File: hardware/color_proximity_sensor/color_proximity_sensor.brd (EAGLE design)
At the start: 48 x 24.8 mm, 69 parts, among them IC1 TCS37725FN, IC2 APDS-9800-021, IC4 LM25011MY, IC5 ATXMEGA64DA-AU, J1 PDI_ATMEL_WIDTH, Q1 16 MHz, T1 BC847CDXV6T1G, T4 BC847CDXV6T1G

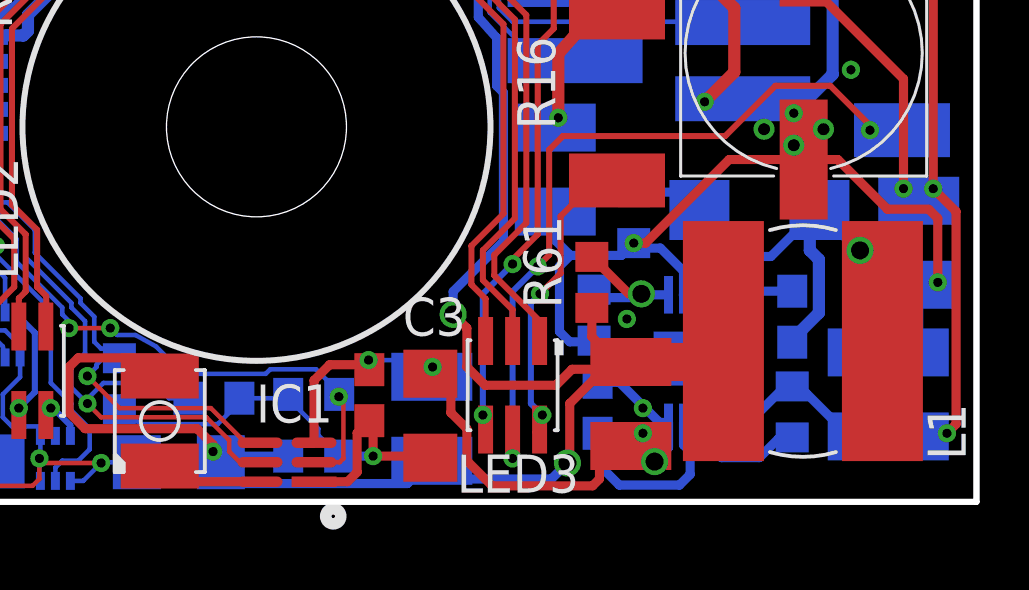
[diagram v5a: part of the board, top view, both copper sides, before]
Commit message: corrected tcs37725 and b160, need rerouting tcs37725
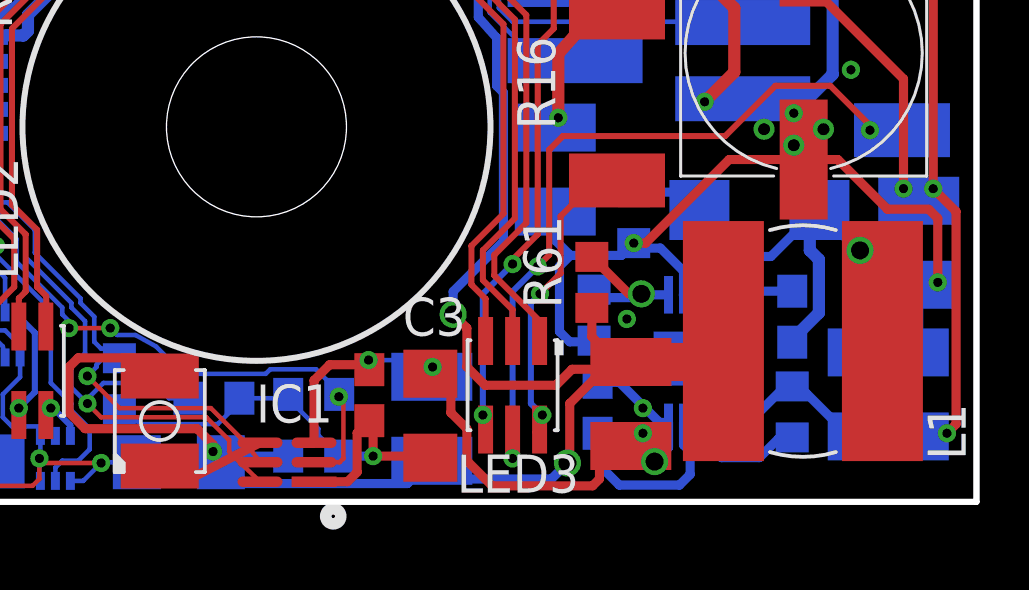
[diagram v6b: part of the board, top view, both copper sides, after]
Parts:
- turned D8 to 0 degrees
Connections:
- net INT_TCS37725_3V3: now also IC1.5; no longer IC1.4
- net N$38: now also D8.C; no longer D8.A
- net N$39: now also D8.A; no longer D8.C
- net N$4: now also IC1.4; no longer IC1.6
- net SDA_3V3: now also IC1.6; no longer IC1.5
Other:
- board text added: "color_prox sens v2"
- board text removed: "color_prox sens v1"
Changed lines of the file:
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@@
 <layers>
 <layer number="1" name="Top" color="4" fill="1" visible="yes" active="yes"/>
-<layer number="16" name="Bottom" color="1" fill="1" visible="yes" active="yes"/>
+<layer number="16" name="Bottom" color="1" fill="1" visible="no" active="yes"/>
 <layer number="17" name="Pads" color="2" fill="1" visible="yes" active="yes"/>
 <layer number="18" name="Vias" color="2" fill="1" visible="yes" active="yes"/>
@@
 <layer number="23" name="tOrigins" color="15" fill="1" visible="yes" active="yes"/>
 <layer number="24" name="bOrigins" color="15" fill="1" visible="yes" active="yes"/>
-<layer number="25" name="tNames" color="7" fill="1" visible="yes" active="yes"/>
+<layer number="25" name="tNames" color="7" fill="1" visible="no" active="yes"/>
 <layer number="26" name="bNames" color="7" fill="1" visible="yes" active="yes"/>
 <layer number="27" name="tValues" color="7" fill="1" visible="no" active="yes"/>
@@
 <layer number="42" name="bRestrict" color="1" fill="10" visible="yes" active="yes"/>
 <layer number="43" name="vRestrict" color="2" fill="10" visible="yes" active="yes"/>
-<layer number="44" name="Drills" color="7" fill="1" visible="yes" active="yes"/>
-<layer number="45" name="Holes" color="7" fill="1" visible="yes" active="yes"/>
+<layer number="44" name="Drills" color="7" fill="1" visible="no" active="yes"/>
+<layer number="45" name="Holes" color="7" fill="1" visible="no" active="yes"/>
 <layer number="46" name="Milling" color="3" fill="1" visible="no" active="yes"/>
 <layer number="47" name="Measures" color="7" fill="1" visible="no" active="yes"/>
@@
 <circle x="24" y="12.5" radius="7.8" width="0.2032" layer="42"/>
 <text x="31.8516" y="20.193" size="1.778" layer="26" rot="MR0">color_prox
-sens v1</text>
+sens v2</text>
 <circle x="24" y="12.5" radius="9" width="0.4064" layer="47"/>
 <circle x="24" y="12.5" radius="7.8" width="0.2" layer="22"/>
@@
 <attribute name="MOUSER" value="581-1210ZG226Z" x="36.479478125" y="3.261359375" size="1.778" layer="27" rot="R270" display="off"/>
 </element>
-<element name="D8" library="robotter_diode" package="SMA" value="B160-13F" x="40.767" y="9.7282" smashed="yes" rot="MR180">
-<attribute name="RS" value="738-4765" x="110.617" y="35.1282" size="1.778" layer="28" rot="MR180" display="off"/>
-<attribute name="NAME" x="40.1762" y="8.7562" size="1.27" layer="26" ratio="10" rot="MR90"/>
-<attribute name="VALUE" x="38.017" y="13.2282" size="1.27" layer="28" ratio="10" rot="MR180"/>
-<attribute name="MOUSER" value="621-B160-F" x="40.767" y="9.7282" size="1.778" layer="28" rot="MR180" display="off"/>
+<element name="D8" library="robotter_diode" package="SMA" value="B160-13F" x="40.767" y="9.7282" smashed="yes" rot="MR0">
+<attribute name="RS" value="738-4765" x="-29.083" y="-15.6718" size="1.778" layer="28" rot="MR0" display="off"/>
+<attribute name="NAME" x="41.3578" y="10.7002" size="1.27" layer="26" ratio="10" rot="MR270"/>
+<attribute name="VALUE" x="43.517" y="6.2282" size="1.27" layer="28" ratio="10" rot="MR0"/>
+<attribute name="MOUSER" value="621-B160-F" x="40.767" y="9.7282" size="1.778" layer="28" rot="MR0" display="off"/>
 </element>
 <element name="L1" library="robotter_inductor" package="SDR0805" value="SDR0805-270KL" x="42.2148" y="5.3594" smashed="yes" rot="R90">
@@
 <attribute name="NAME" x="2.6416" y="21.4122" size="1.27" layer="26" rot="MR90"/>
 <attribute name="VALUE" x="-1.0922" y="22.098" size="1.27" layer="28" rot="MR90"/>
-<attribute name="MOUSER" value="652-CR0805FX-1502ELF" x="1.4478" y="22.733" size="1.778" layer="28" rot="MR90" display="off"/>
+<attribute name="MOUSER" value="660-RK73H2ATTD1502F" x="1.4478" y="22.733" size="1.778" layer="28" rot="MR90" display="off"/>
 </element>
 <element name="R14" library="robotter_resistor" package="R0805" value="1k" x="1.4478" y="22.7076" smashed="yes" rot="R270">
@@
 <attribute name="NAME" x="26.543" y="2.159" size="1.27" layer="100" rot="MR0"/>
 <attribute name="VALUE" x="26.543" y="-0.381" size="1.27" layer="28" rot="MR0"/>
-<attribute name="MOUSER" value="279-CRG0603F22R" x="25.908" y="1.524" size="1.778" layer="28" rot="MR0" display="off"/>
+<attribute name="MOUSER" value="660-RK73H1JTTD22R0F" x="25.908" y="1.524" size="1.778" layer="28" rot="MR0" display="off"/>
 </element>
 <element name="IC2" library="robotter_ic" package="APDS-9800" value="APDS-9800-021" x="10.3886" y="4.9022" smashed="yes">
@@
 <attribute name="NAME" x="10.9474" y="2.794" size="1.27" layer="103" rot="MR0"/>
 <attribute name="VALUE" x="10.6426" y="1.4732" size="1.27" layer="28" rot="MR0"/>
-<attribute name="MOUSER" value="279-CRG0603F22R" x="10.0076" y="3.3782" size="1.778" layer="28" rot="MR0" display="off"/>
+<attribute name="MOUSER" value="660-RK73H1JTTD22R0F" x="10.0076" y="3.3782" size="1.778" layer="28" rot="MR0" display="off"/>
 </element>
 <element name="R4" library="robotter_resistor" package="R0603" value="22 ohms" x="10.0076" y="1.3462" smashed="yes" rot="MR0">
@@
 <attribute name="NAME" x="11.176" y="0.762" size="1.27" layer="103" rot="MR0"/>
 <attribute name="VALUE" x="10.6426" y="-0.5588" size="1.27" layer="28" rot="MR0"/>
-<attribute name="MOUSER" value="279-CRG0603F22R" x="10.0076" y="1.3462" size="1.778" layer="28" rot="MR0" display="off"/>
+<attribute name="MOUSER" value="660-RK73H1JTTD22R0F" x="10.0076" y="1.3462" size="1.778" layer="28" rot="MR0" display="off"/>
 </element>
 <element name="R5" library="robotter_resistor" package="R0603" value="10K-F" x="11.9126" y="9.7282" smashed="yes">
@@
 <signal name="N$38">
 <contactref element="IC4" pad="9"/>
-<contactref element="D8" pad="A"/>
+<contactref element="D8" pad="C"/>
 <contactref element="C32" pad="2"/>
 <contactref element="L1" pad="1"/>
@@
 <signal name="N$39">
 <contactref element="IC4" pad="8"/>
-<contactref element="D8" pad="C"/>
+<contactref element="D8" pad="A"/>
 <contactref element="R22" pad="2"/>
 <wire x1="38.735" y1="6.9022" x2="38.735" y2="9.6962" width="0.3048" layer="16"/>
@@
 <signal name="INT_TCS37725_3V3">
 <contactref element="R1" pad="1"/>
-<contactref element="IC1" pad="4"/>
+<contactref element="IC1" pad="5"/>
 <contactref element="IC5" pad="27"/>
 <wire x1="19.431" y1="4.787" x2="19.265" y2="4.953" width="0.1524" layer="16"/>
@@
 <wire x1="19.3684" y1="4.787" x2="19.431" y2="4.787" width="0.1524" layer="16"/>
 <wire x1="22.479" y1="3.1242" x2="23.6324" y2="1.9708" width="0.1524" layer="1"/>
-<wire x1="23.6324" y1="1.9708" x2="24.119" y2="1.9708" width="0.1524" layer="1"/>
+<wire x1="23.6324" y1="1.9708" x2="24.119" y2="1.3208" width="0.1524" layer="1"/>
 </signal>
 <signal name="SDA_3V3">
-<contactref element="IC1" pad="5"/>
+<contactref element="IC1" pad="6"/>
 <contactref element="R25" pad="1"/>
 <contactref element="IC5" pad="28"/>
@@
 <wire x1="23.0886" y1="2.0574" x2="23.0886" y2="1.6764" width="0.1524" layer="1"/>
 <wire x1="23.0886" y1="1.6764" x2="23.4442" y2="1.3208" width="0.1524" layer="1"/>
-<wire x1="23.4442" y1="1.3208" x2="24.119" y2="1.3208" width="0.1524" layer="1"/>
+<wire x1="23.4442" y1="1.3208" x2="24.119" y2="0.6708" width="0.1524" layer="1"/>
 </signal>
 <signal name="SCL_3V3">
@@
 </signal>
 <signal name="N$4">
-<contactref element="IC1" pad="6"/>
+<contactref element="IC1" pad="4"/>
 <contactref element="LED1" pad="C"/>
 <wire x1="21.2076" y1="1.0668" x2="20.7772" y2="1.1924" width="0.3048" layer="1"/>
 <wire x1="21.2076" y1="1.0668" x2="21.6036" y2="0.6708" width="0.3048" layer="1"/>
-<wire x1="21.6036" y1="0.6708" x2="24.119" y2="0.6708" width="0.3048" layer="1"/>
+<wire x1="21.6036" y1="0.6708" x2="24.119" y2="1.9708" width="0.3048" layer="1"/>
 </signal>
 <signal name="TCS_VCC">

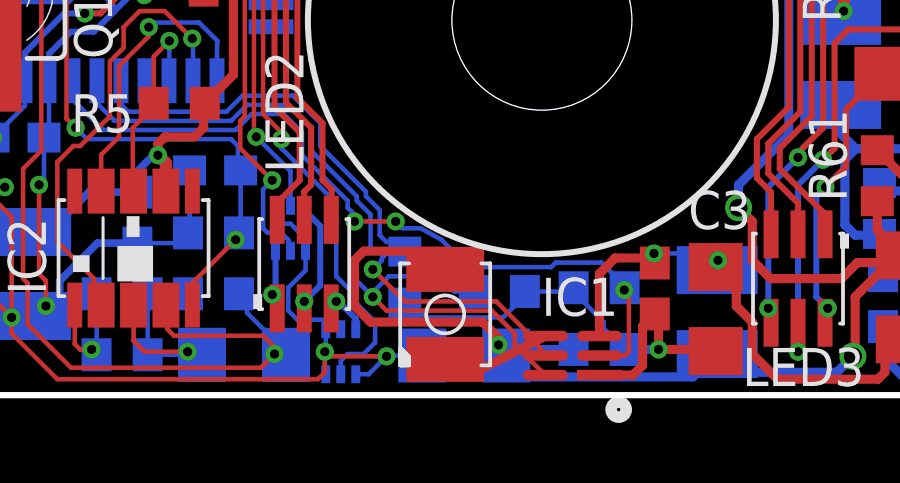
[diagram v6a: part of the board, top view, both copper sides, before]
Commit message: v2 rerouted and ic5 (atxmega) value modified
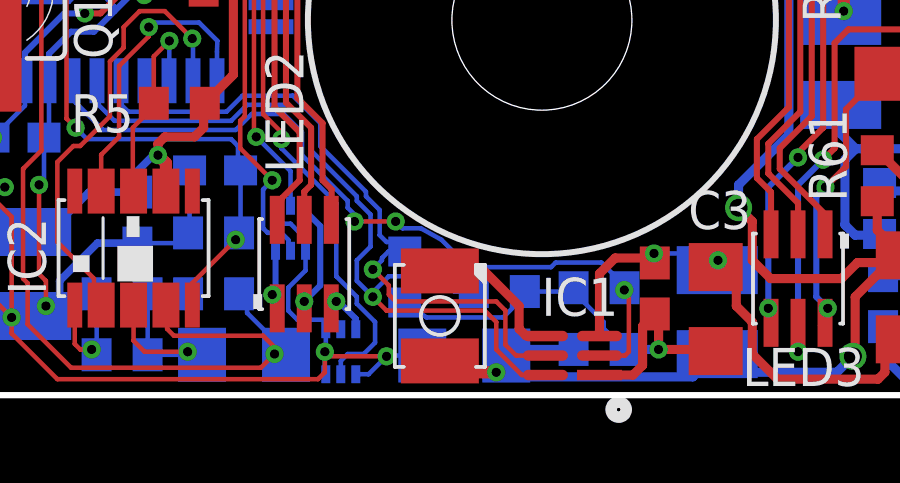
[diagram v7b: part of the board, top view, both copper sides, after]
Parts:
- IC5: value ATXMEGA64DA-AU -> ATXMEGA64D4-AU
- moved LED1 0.18 mm to (20.6, 2.64), turned to 180 degrees
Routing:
- net +3V3: track 154.1 -> 148.3 mm
- net N$4: track 3.84 -> 4.87 mm
- net INT_TCS37725_3V3: track 22.8 -> 23.6 mm
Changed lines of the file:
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@@
 <layers>
 <layer number="1" name="Top" color="4" fill="1" visible="yes" active="yes"/>
-<layer number="16" name="Bottom" color="1" fill="1" visible="no" active="yes"/>
+<layer number="16" name="Bottom" color="1" fill="1" visible="yes" active="yes"/>
 <layer number="17" name="Pads" color="2" fill="1" visible="yes" active="yes"/>
 <layer number="18" name="Vias" color="2" fill="1" visible="yes" active="yes"/>
@@
 <attribute name="MOUSER" value="810-C3216X7R1E105K-6" x="29.7942" y="2.8702" size="1.778" layer="27" rot="R90" display="off"/>
 </element>
-<element name="LED1" library="robotter_diode" package="SFH4253" value="SFH 4253" x="20.7772" y="2.6924" smashed="yes">
-<attribute name="RS" value="665-5495" x="52.5272" y="-84.9376" size="1.778" layer="27" display="off"/>
-<attribute name="NAME" x="18.6944" y="-1.5494" size="1.27" layer="100" ratio="10"/>
-<attribute name="VALUE" x="24.5872" y="0.4064" size="1.27" layer="27" ratio="10" rot="R90"/>
-<attribute name="MOUSER" value="720-SFH4253-Z " x="20.7772" y="2.6924" size="1.778" layer="27" display="off"/>
+<element name="LED1" library="robotter_diode" package="SFH4253" value="SFH 4253" x="20.5994" y="2.6416" smashed="yes" rot="R180">
+<attribute name="RS" value="665-5495" x="-11.1506" y="90.2716" size="1.778" layer="27" rot="R180" display="off"/>
+<attribute name="NAME" x="22.6822" y="6.8834" size="1.27" layer="100" ratio="10" rot="R180"/>
+<attribute name="VALUE" x="16.7894" y="4.9276" size="1.27" layer="27" ratio="10" rot="R270"/>
+<attribute name="MOUSER" value="720-SFH4253-Z " x="20.5994" y="2.6416" size="1.778" layer="27" rot="R180" display="off"/>
 </element>
 <element name="C4" library="robotter_capacitor" package="C1206" value="1µF 25V" x="21.4122" y="1.3208" smashed="yes" rot="MR0">
@@
 <attribute name="MOUSER" value="279-35201K0JT" x="37.973" y="22.6568" size="1.778" layer="27" display="off"/>
 </element>
-<element name="IC5" library="robotter_ic" package="TQFP44" value="ATXMEGA64DA-AU" x="9.1694" y="16.2814" smashed="yes" rot="MR270">
+<element name="IC5" library="robotter_ic" package="TQFP44" value="ATXMEGA64D4-AU" x="9.1694" y="16.2814" smashed="yes" rot="MR270">
 <attribute name="RS" value="" x="19.3294" y="-28.1686" size="1.778" layer="28" rot="MR270" display="off"/>
 <attribute name="NAME" x="9.9314" y="24.7396" size="1.778" layer="26" rot="MR180"/>
@@
 <wire x1="35.8576375" y1="4.826" x2="36.479478125" y2="4.661359375" width="0.3048" layer="1"/>
 <contactref element="J1" pad="2"/>
-<wire x1="20.7772" y1="4.1924" x2="20.8548" y2="4.8006" width="0.1524" layer="1"/>
-<wire x1="20.8548" y1="4.8006" x2="18.0594" y2="4.8006" width="0.3048" layer="1"/>
-<wire x1="18.0594" y1="4.8006" x2="17.7546" y2="4.4958" width="0.3048" layer="1"/>
-<wire x1="17.7546" y1="4.4958" x2="17.7546" y2="2.9718" width="0.3048" layer="1"/>
-<wire x1="17.7546" y1="2.9718" x2="18.288" y2="2.4384" width="0.3048" layer="1"/>
-<wire x1="18.288" y1="2.4384" x2="22.0218" y2="2.4384" width="0.3048" layer="1"/>
 <wire x1="22.8122" y1="1.3208" x2="22.9108" y2="1.3208" width="0.3048" layer="16"/>
 <wire x1="22.9108" y1="1.3208" x2="23.3172" y2="1.6764" width="0.3048" layer="16"/>
-<wire x1="23.3172" y1="1.6764" x2="22.5552" y2="1.6764" width="0.3048" layer="16"/>
-<via x="22.5552" y="1.6764" extent="1-16" drill="0.3048" shape="octagon"/>
-<wire x1="22.5552" y1="1.6764" x2="22.5552" y2="1.905" width="0.3048" layer="1"/>
-<wire x1="22.5552" y1="1.905" x2="22.0218" y2="2.4384" width="0.3048" layer="1"/>
+<wire x1="23.3172" y1="1.6764" x2="22.479" y2="0.762" width="0.3048" layer="16"/>
+<via x="22.479" y="0.762" extent="1-16" drill="0.3048" shape="octagon"/>
 <wire x1="1.2192" y1="12.5848" x2="1.2192" y2="19.3548" width="0.1524" layer="16"/>
 <via x="1.2192" y="19.3548" extent="1-16" drill="0.3048" shape="octagon"/>
@@
 <wire x1="28.2702" y1="22.2504" x2="19.3548" y2="22.2504" width="0.3048" layer="16"/>
 <wire x1="19.3548" y1="22.2504" x2="19.2024" y2="22.098" width="0.3048" layer="16"/>
+<wire x1="22.479" y1="0.762" x2="20.4978" y2="0.762" width="0.4064" layer="1"/>
+<wire x1="20.4978" y1="0.762" x2="20.4216" y2="1.3716" width="0.4064" layer="1"/>
+<wire x1="20.4216" y1="1.3716" x2="21.487" y2="1.1416" width="0.4064" layer="1"/>
+<wire x1="21.487" y1="1.1416" x2="20.5994" y2="1.1416" width="0.4064" layer="1"/>
 </signal>
 <signal name="BATTERY_MONITOR_0-1V">
@@
 <contactref element="IC5" pad="27"/>
 <wire x1="19.431" y1="4.787" x2="19.265" y2="4.953" width="0.1524" layer="16"/>
-<wire x1="22.479" y1="3.1242" x2="19.431" y2="3.1242" width="0.1524" layer="1"/>
-<wire x1="19.431" y1="3.1242" x2="18.3642" y2="4.191" width="0.1524" layer="1"/>
+<wire x1="22.479" y1="3.1242" x2="19.1262" y2="3.1242" width="0.1524" layer="1"/>
+<wire x1="19.1262" y1="3.1242" x2="18.8976" y2="3.3528" width="0.1524" layer="1"/>
+<wire x1="18.8976" y1="3.3528" x2="18.8976" y2="3.6576" width="0.1524" layer="1"/>
+<wire x1="18.8976" y1="3.6576" x2="18.3642" y2="4.191" width="0.1524" layer="1"/>
 <via x="18.3642" y="4.191" extent="1-16" drill="0.3048" shape="octagon"/>
 <wire x1="18.3642" y1="4.191" x2="18.669" y2="4.4958" width="0.1524" layer="16"/>
@@
 <wire x1="19.05" y1="5.1054" x2="19.3684" y2="4.787" width="0.1524" layer="16"/>
 <wire x1="19.3684" y1="4.787" x2="19.431" y2="4.787" width="0.1524" layer="16"/>
-<wire x1="22.479" y1="3.1242" x2="23.6324" y2="1.9708" width="0.1524" layer="1"/>
-<wire x1="23.6324" y1="1.9708" x2="24.119" y2="1.3208" width="0.1524" layer="1"/>
+<wire x1="24.119" y1="1.3208" x2="23.1394" y2="1.3208" width="0.1524" layer="1"/>
+<wire x1="23.1394" y1="1.3208" x2="22.7838" y2="1.6764" width="0.1524" layer="1"/>
+<wire x1="22.7838" y1="1.6764" x2="22.7838" y2="2.8194" width="0.1524" layer="1"/>
+<wire x1="22.7838" y1="2.8194" x2="22.479" y2="3.1242" width="0.1524" layer="1"/>
 </signal>
 <signal name="SDA_3V3">
@@
 <contactref element="R25" pad="1"/>
 <contactref element="IC5" pad="28"/>
-<wire x1="22.3266" y1="2.8194" x2="18.8214" y2="2.8194" width="0.1524" layer="1"/>
+<wire x1="22.098" y1="2.8194" x2="18.8214" y2="2.8194" width="0.1524" layer="1"/>
 <wire x1="18.8214" y1="2.8194" x2="18.3642" y2="3.2766" width="0.1524" layer="1"/>
 <via x="18.3642" y="3.2766" extent="1-16" drill="0.3048" shape="octagon"/>
@@
 <wire x1="17.8308" y1="6.477" x2="18.288" y2="6.0198" width="0.1524" layer="16"/>
 <wire x1="18.288" y1="6.0198" x2="18.288" y2="4.953" width="0.1524" layer="16"/>
-<wire x1="22.3266" y1="2.8194" x2="23.0886" y2="2.0574" width="0.1524" layer="1"/>
-<wire x1="23.0886" y1="2.0574" x2="23.0886" y2="1.6764" width="0.1524" layer="1"/>
-<wire x1="23.0886" y1="1.6764" x2="23.4442" y2="1.3208" width="0.1524" layer="1"/>
-<wire x1="23.4442" y1="1.3208" x2="24.119" y2="0.6708" width="0.1524" layer="1"/>
+<wire x1="22.098" y1="2.8194" x2="22.479" y2="2.4384" width="0.1524" layer="1"/>
+<wire x1="22.479" y1="2.4384" x2="22.479" y2="1.524" width="0.1524" layer="1"/>
+<wire x1="23.3322" y1="0.6708" x2="24.119" y2="0.6708" width="0.1524" layer="1"/>
+<wire x1="23.3322" y1="0.6708" x2="22.479" y2="1.524" width="0.1524" layer="1"/>
 </signal>
 <signal name="SCL_3V3">
@@
 <contactref element="IC1" pad="4"/>
 <contactref element="LED1" pad="C"/>
-<wire x1="21.2076" y1="1.0668" x2="20.7772" y2="1.1924" width="0.3048" layer="1"/>
-<wire x1="21.2076" y1="1.0668" x2="21.6036" y2="0.6708" width="0.3048" layer="1"/>
-<wire x1="21.6036" y1="0.6708" x2="24.119" y2="1.9708" width="0.3048" layer="1"/>
+<wire x1="20.5994" y1="4.1416" x2="22.0712" y2="4.1416" width="0.3048" layer="1"/>
+<wire x1="22.0712" y1="4.1416" x2="23.241" y2="2.9718" width="0.3048" layer="1"/>
+<wire x1="23.241" y1="2.9718" x2="23.241" y2="2.2098" width="0.3048" layer="1"/>
+<wire x1="23.241" y1="2.2098" x2="23.4696" y2="1.9812" width="0.3048" layer="1"/>
+<wire x1="23.4696" y1="1.9812" x2="24.1086" y2="1.9812" width="0.3048" layer="1"/>
+<wire x1="24.1086" y1="1.9812" x2="24.119" y2="1.9708" width="0.3048" layer="1"/>
 </signal>
 <signal name="TCS_VCC">
